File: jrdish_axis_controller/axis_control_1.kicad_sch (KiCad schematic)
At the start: 36 parts, among them CN1 KF2EDGR-2.54-9P, CN2 KF2EDGR-2.54-6P, Q5 BSS138, Q6 BSS138

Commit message: Verion that works, PCB assembeled ant testing
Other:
- note added: "The encoder is missing pulses at higher speeds. Claude Fable 5 suggests changing to 1k ohm and 1nF, τ = 1 µs."
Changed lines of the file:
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@@
+		)
+	)
+	(text "The encoder is missing pulses at higher speeds. \nClaude Fable 5 suggests changing to 1k ohm and\n1nF, τ = 1 µs."
+		(exclude_from_sim no)
+		(at 29.972 31.75 0)
+		(effects
+			(font
+				(size 3.048 3.048)
+			)
+			(justify left)
 		)
 	)

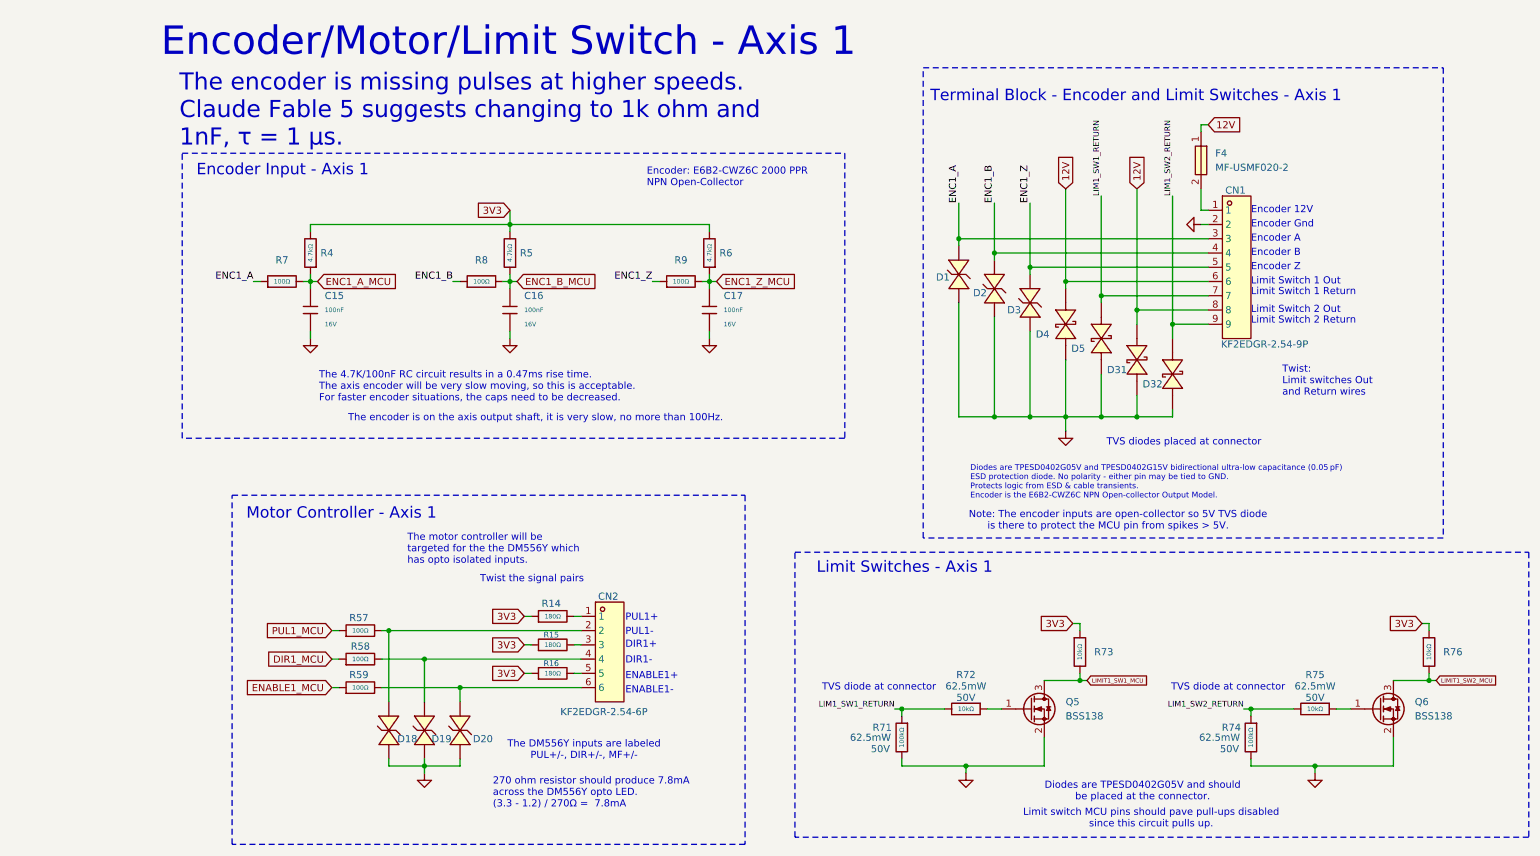
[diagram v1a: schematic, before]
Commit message: Updates for replacing 10k resistors and encoder RC.
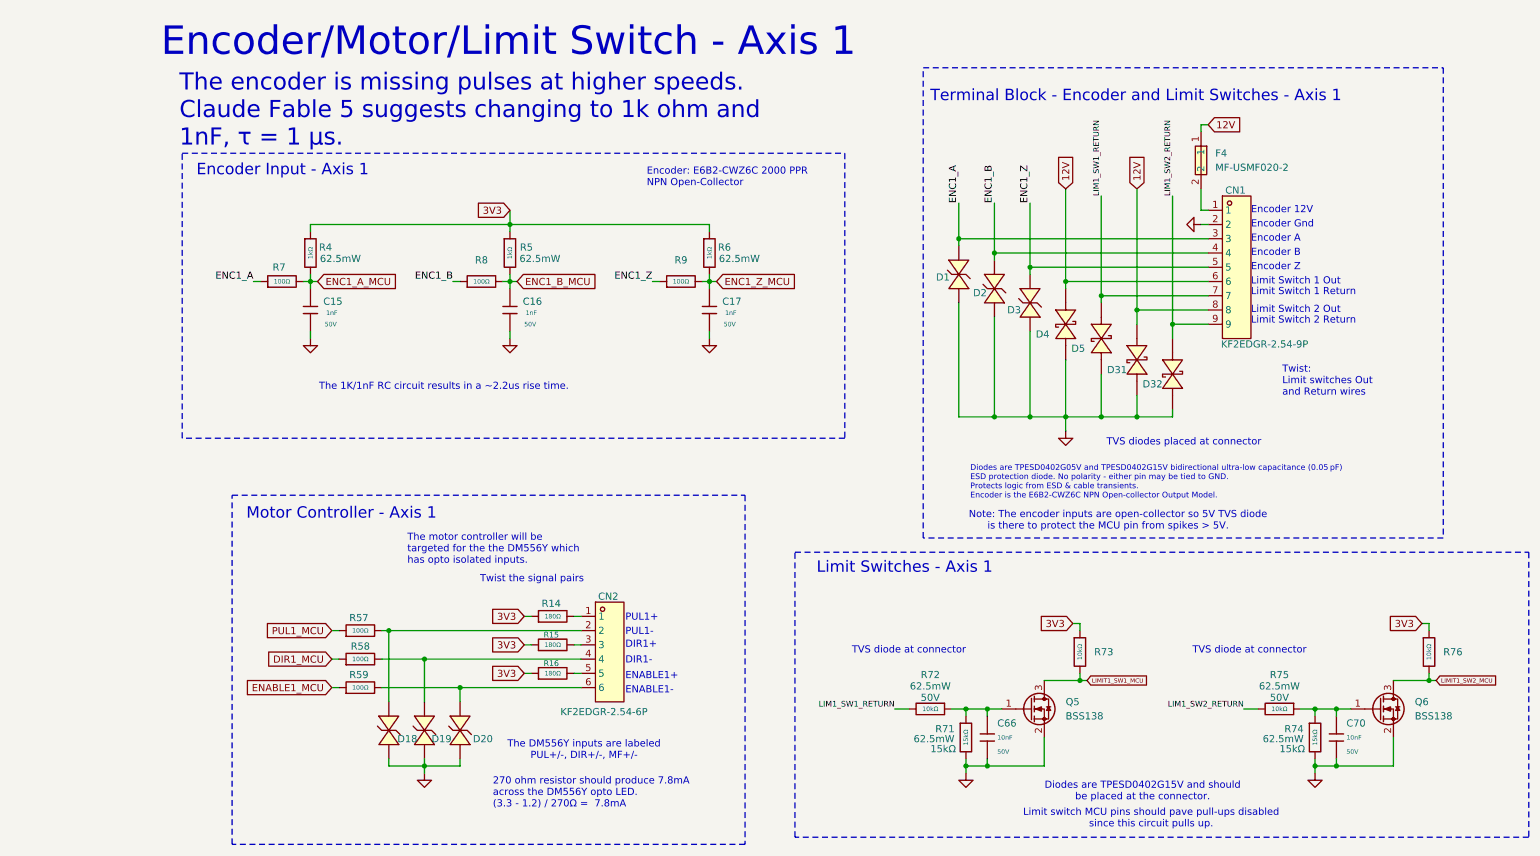
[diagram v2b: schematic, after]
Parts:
- removed C15, C16, C17: 100nF, PCM_JLCPCB:C_0402, symbol PCM_JLCPCB-Capacitors:0402,100nF
- removed R4, R5, R6: 4.7kΩ, PCM_JLCPCB:R_0402, symbol PCM_JLCPCB-Resistors:0402,4.7kΩ
- removed R71, R74: 100kΩ, PCM_JLCPCB:R_0402, symbol PCM_JLCPCB-Resistors:0402,100kΩ
- added C15, C16, C17: 1nF, PCM_JLCPCB:C_0402, symbol PCM_JLCPCB-Capacitors:0402,1nF
- added C66, C70: 10nF, PCM_JLCPCB:C_0603, symbol PCM_JLCPCB-Capacitors:0603,10nF
- added R4, R5, R6: 1kΩ, PCM_JLCPCB:R_0402, symbol PCM_JLCPCB-Resistors:0402,1kΩ
- added R71, R74: 15kΩ, PCM_JLCPCB:R_0402, symbol PCM_JLCPCB-Resistors:0402,15kΩ
- Q5, Q6: KiLib_Generator (none) -> package/gullwing
- R57, R58, R59: Field4 (none) -> ${REFERENCE}
- R72, R73, R75, R76: Field4 (none) -> ${REFERENCE}; LCSC C25744 -> C173683
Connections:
- net 3V3: now also R4.1, R5.1, R6.1
- net ENC1_A_MCU: now also C15.1, R4.2
- net ENC1_B_MCU: now also C16.1, R5.2
- net ENC1_Z_MCU: now also C17.1, R6.2
- net GND: now also C15.2, C16.2, C17.2, C66.2, C70.2, R71.2, R74.2
- net at Q5.1 (G), R72.1: now also C66.1, R71.1
- net at Q6.1 (G), R75.1: now also C70.1, R74.1
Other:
- note added: "Diodes are TPESD0402G15V and should be placed at the connector."
- note added: "The 1K/1nF RC circuit results in a ~2.2us rise time."
- note removed: "Diodes are TPESD0402G05V and should be placed at the connector."
- note removed: "The 4.7K/100nF RC circuit results in a 0.47ms rise time. The axis encoder will be very slow moving, so this is acceptable. For faster encoder situations, the caps need to be decreased."
- note removed: "The encoder is on the axis output shaft, it is very slow, no more than 100Hz."
- moved on the sheet: R72, R75
